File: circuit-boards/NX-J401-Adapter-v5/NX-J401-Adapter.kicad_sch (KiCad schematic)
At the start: 20 parts, among them J1 18V_OUT, J2 NX BUTTON, J3 Power, SW1 RECOVERY, SW2 RESET

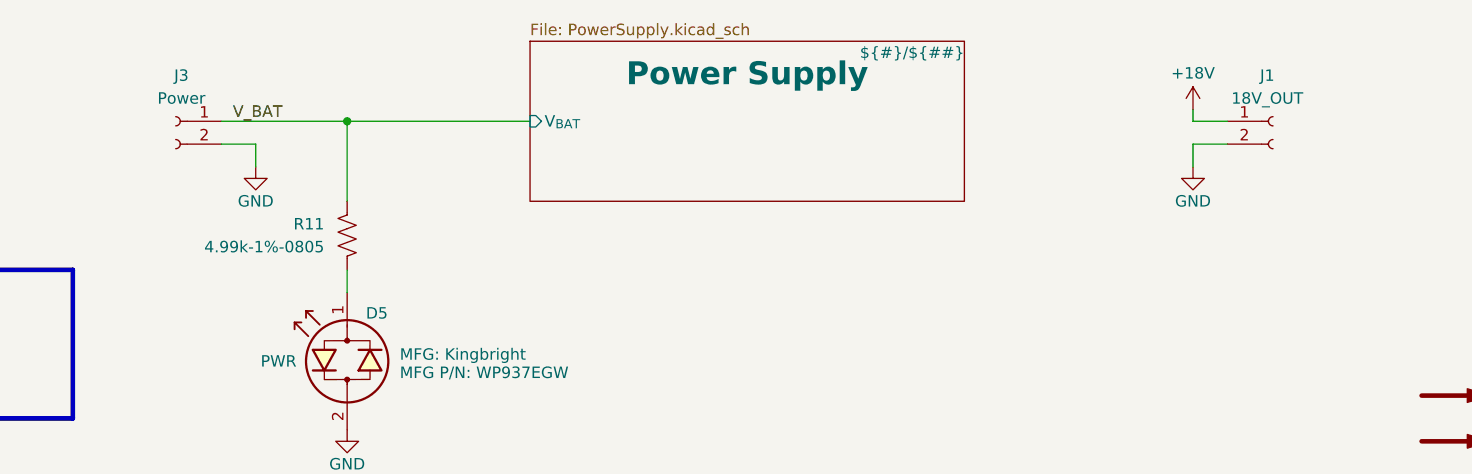
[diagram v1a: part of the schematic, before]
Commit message: Add over voltage protection to NX adapter circuit. Also reduce component height
Signed-off-by: Scott Berman <sgberman1@gmail.com>
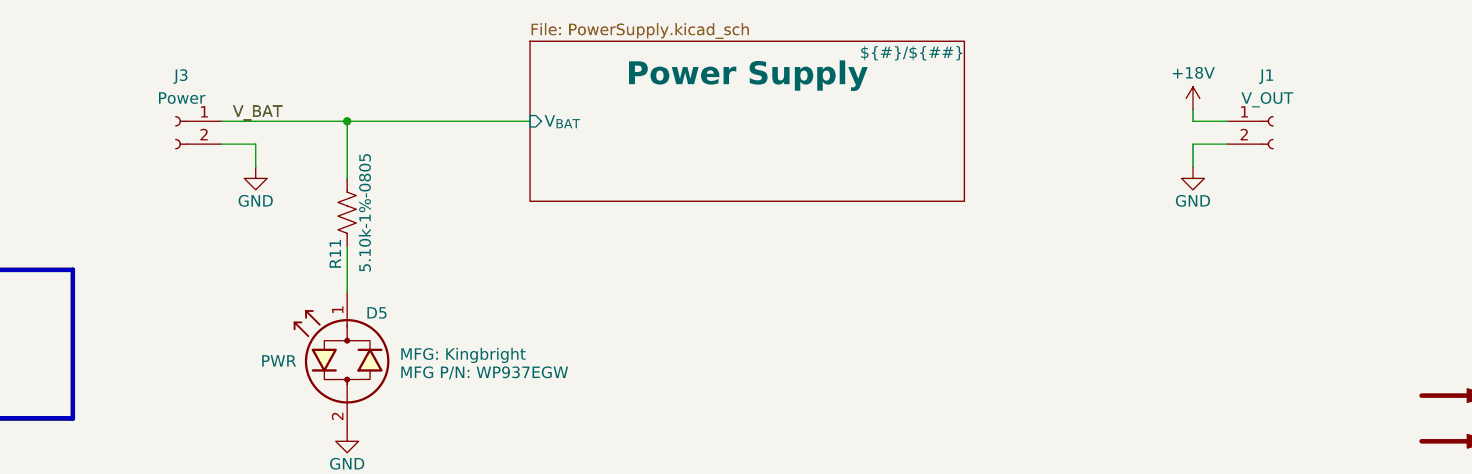
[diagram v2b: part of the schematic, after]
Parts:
- J1: value 18V_OUT -> V_OUT; footprint NX-J401-Adapter:CONN_69140872_WRE -> NX-J401-Adapter:Weidmuller-1824740000; DIST P/N 732-691408720002B-ND -> 281-2110-ND; MFG Würth Elektronik -> Weidmuller; MFG P/N 691408720002B -> 1824740000
- J3: footprint NX-J401-Adapter:Wurth-691406510002B -> NX-J401-Adapter:Weidmuller-1824740000; DIST P/N 732-691406510002B-ND -> 281-2110-ND; MFG Wurth -> Weidmuller; MFG P/N 691406510002B -> 1824740000
- R11: value 4.99k-1%-0805 -> 5.10k-1%-0805; DIST P/N 311-499CRCT-ND -> 311-5.10KCRCT-ND; MFG P/N RC0805FR-07499RL -> RC0805FR-075K1L
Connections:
- net V_BAT: now also R11.1; no longer R11.2
- net at D5.1 (KA): now also R11.2; no longer R11.1
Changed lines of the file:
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@@
 	(wire
 		(pts
-			(xy 161.29 73.66) (xy 161.29 82.55)
+			(xy 161.29 73.66) (xy 161.29 80.01)
 		)
 		(stroke
@@
 	(wire
 		(pts
-			(xy 161.29 90.17) (xy 161.29 92.71)
+			(xy 161.29 87.63) (xy 161.29 92.71)
 		)
 		(stroke
@@
 	)
 	(symbol
-		(lib_id "Device:R_US")
-		(at 161.29 86.36 0)
-		(mirror x)
-		(unit 1)
-		(exclude_from_sim no)
-		(in_bom yes)
-		(on_board yes)
-		(dnp no)
-		(property "Reference" "R11"
-			(at 158.75 85.09 0)
-			(effects
-				(font
-					(size 1.27 1.27)
-				)
-				(justify right)
-			)
-		)
-		(property "Value" "4.99k-1%-0805"
-			(at 158.75 87.63 0)
-			(effects
-				(font
-					(size 1.27 1.27)
-				)
-				(justify right)
-			)
-		)
-		(property "Footprint" "Resistor_SMD:R_0805_2012Metric"
-			(at 162.306 86.106 90)
-			(effects
-				(font
-					(size 1.27 1.27)
-				)
-				(hide yes)
-			)
-		)
-		(property "Datasheet" "Components/YageoPYu-RC_Group_51_RoHS_L_12.pdf"
-			(at 161.29 86.36 0)
-			(effects
-				(font
-					(size 1.27 1.27)
-				)
-				(hide yes)
-			)
-		)
-		(property "Description" ""
-			(at 161.29 86.36 0)
-			(effects
-				(font
-					(size 1.27 1.27)
-				)
-				(hide yes)
-			)
-		)
-		(property "MFG" "Yageo"
-			(at 161.29 86.36 0)
-			(effects
-				(font
-					(size 1.27 1.27)
-				)
-				(hide yes)
-			)
-		)
-		(property "MFG P/N" "RC0805FR-07499RL"
-			(at 161.29 86.36 0)
-			(effects
-				(font
-					(size 1.27 1.27)
-				)
-				(hide yes)
-			)
-		)
-		(property "DIST" "Digikey"
-			(at 161.29 86.36 0)
-			(effects
-				(font
-					(size 1.27 1.27)
-				)
-				(hide yes)
-			)
-		)
-		(property "DIST P/N" "311-499CRCT-ND"
-			(at 161.29 86.36 0)
-			(effects
-				(font
-					(size 1.27 1.27)
-				)
-				(hide yes)
-			)
-		)
-		(pin "1"
-		)
-		(pin "2"
-		)
-		(instances
-			(project "PI-Power-Board"
-				(path "/2707d6e5-f0fd-4132-ae41-e0b291f42ef6/feeb2d6c-4828-41f4-95de-5c15de403137"
-					(reference "R17")
-					(unit 1)
-				)
-			)
-			(project "NX-J401-Adapter"
-				(path "/cc31ce4b-09ab-4aea-a1d3-ed84696ba658"
-					(reference "R11")
-					(unit 1)
-				)
-			)
-		)
-	)
-	(symbol
 		(lib_id "Device:LED_Dual_Bidirectional")
 		(at 161.29 100.33 90)
@@
 	)
 	(symbol
+		(lib_id "Connector:Conn_01x02_Socket")
+		(at 264.16 73.66 0)
+		(unit 1)
+		(exclude_from_sim no)
+		(in_bom yes)
+		(on_board yes)
+		(dnp no)
+		(property "Reference" "J1"
+			(at 263.525 68.58 0)
+			(effects
+				(font
+					(size 1.27 1.27)
+				)
+			)
+		)
+		(property "Value" "V_OUT"
+			(at 263.525 71.12 0)
+			(effects
+				(font
+					(size 1.27 1.27)
+				)
+			)
+		)
+		(property "Footprint" "NX-J401-Adapter:Weidmuller-1824740000"
+			(at 264.16 73.66 0)
+			(effects
+				(font
+					(size 1.27 1.27)
+				)
+				(hide yes)
+			)
+		)
+		(property "Datasheet" "Components/Wurth-0691406510002B.pdf"
+			(at 264.16 73.66 0)
+			(effects
+				(font
+					(size 1.27 1.27)
+				)
+				(hide yes)
+			)
+		)
+		(property "Description" ""
+			(at 264.16 73.66 0)
+			(effects
+				(font
+					(size 1.27 1.27)
+				)
+				(hide yes)
+			)
+		)
+		(property "MFG" "Weidmuller"
+			(at 264.16 73.66 0)
+			(effects
+				(font
+					(size 1.27 1.27)
+				)
+				(hide yes)
+			)
+		)
+		(property "MFG P/N" "1824740000"
+			(at 264.16 73.66 0)
+			(effects
+				(font
+					(size 1.27 1.27)
+				)
+				(hide yes)
+			)
+		)
+		(property "DIST" "Digikey"
+			(at 264.16 73.66 0)
+			(effects
+				(font
+					(size 1.27 1.27)
+				)
+				(hide yes)
+			)
+		)
+		(property "DIST P/N" "281-2110-ND"
+			(at 264.16 73.66 0)
+			(effects
+				(font
+					(size 1.27 1.27)
+				)
+				(hide yes)
+			)
+		)
+		(pin "1"
+		)
+		(pin "2"
+		)
+		(instances
+			(project "NX-J401-Adapter"
+				(path "/cc31ce4b-09ab-4aea-a1d3-ed84696ba658"
+					(reference "J1")
+					(unit 1)
+				)
+			)
+		)
+	)
+	(symbol
 		(lib_id "Graphic:SYM_Arrow_Large")
 		(at 284.48 114.3 0)
@@
 	)
 	(symbol
+		(lib_id "Device:R_US")
+		(at 161.29 83.82 0)
+		(unit 1)
+		(exclude_from_sim no)
+		(in_bom yes)
+		(on_board yes)
+		(dnp no)
+		(property "Reference" "R11"
+			(at 160.02 88.392 90)
+			(effects
+				(font
+					(size 1.27 1.27)
+				)
+			)
+		)
+		(property "Value" "5.10k-1%-0805"
+			(at 163.322 83.82 90)
+			(effects
+				(font
+					(size 1.27 1.27)
+				)
+			)
+		)
+		(property "Footprint" "Resistor_SMD:R_0805_2012Metric"
+			(at 162.306 84.074 90)
+			(effects
+				(font
+					(size 1.27 1.27)
+				)
+				(hide yes)
+			)
+		)
+		(property "Datasheet" "Components/YageoPYu-RC_Group_51_RoHS_L_12.pdf"
+			(at 161.29 83.82 0)
+			(effects
+				(font
+					(size 1.27 1.27)
+				)
+				(hide yes)
+			)
+		)
+		(property "Description" ""
+			(at 161.29 83.82 0)
+			(effects
+				(font
+					(size 1.27 1.27)
+				)
+				(hide yes)
+			)
+		)
+		(property "MFG" "Yageo"
+			(at 161.29 83.82 0)
+			(effects
+				(font
+					(size 1.27 1.27)
+				)
+				(hide yes)
+			)
+		)
+		(property "MFG P/N" "RC0805FR-075K1L"
+			(at 161.29 83.82 0)
+			(effects
+				(font
+					(size 1.27 1.27)
+				)
+				(hide yes)
+			)
+		)
+		(property "DIST" "Digikey"
+			(at 161.29 83.82 0)
+			(effects
+				(font
+					(size 1.27 1.27)
+				)
+				(hide yes)
+			)
+		)
+		(property "DIST P/N" "311-5.10KCRCT-ND"
+			(at 161.29 83.82 0)
+			(effects
+				(font
+					(size 1.27 1.27)
+				)
+				(hide yes)
+			)
+		)
+		(pin "1"
+		)
+		(pin "2"
+		)
+		(instances
+			(project "NX-J401-Adapter"
+				(path "/cc31ce4b-09ab-4aea-a1d3-ed84696ba658"
+					(reference "R11")
+					(unit 1)
+				)
+			)
+		)
+	)
+	(symbol
 		(lib_id "power:GND")
 		(at 255.27 78.74 0)
@@
 			)
 		)
-		(property "Footprint" "NX-J401-Adapter:Wurth-691406510002B"
+		(property "Footprint" "NX-J401-Adapter:Weidmuller-1824740000"
 			(at 142.24 73.66 0)
 			(effects
@@
 			)
 		)
-		(property "MFG" "Wurth"
+		(property "MFG" "Weidmuller"
 			(at 142.24 73.66 0)
 			(effects
@@
 			)
 		)
-		(property "MFG P/N" "691406510002B"
+		(property "MFG P/N" "1824740000"
 			(at 142.24 73.66 0)
 			(effects
@@
 			)
 		)
-		(property "DIST P/N" "732-691406510002B-ND"
+		(property "DIST P/N" "281-2110-ND"
 			(at 142.24 73.66 0)
 			(effects
@@
 					(unit 1)
 				)
-			)
-		)
-	)
-	(symbol
-		(lib_id "Connector:Conn_01x02_Socket")
-		(at 264.16 73.66 0)
-		(unit 1)
-		(exclude_from_sim no)
-		(in_bom yes)
-		(on_board yes)
-		(dnp no)
-		(property "Reference" "J1"
-			(at 263.525 68.58 0)
-			(effects
-				(font
-					(size 1.27 1.27)
-				)
-			)
-		)
-		(property "Value" "18V_OUT"
-			(at 263.525 71.12 0)
-			(effects
-				(font
-					(size 1.27 1.27)
-				)
-			)
-		)
-		(property "Footprint" "NX-J401-Adapter:CONN_69140872_WRE"
-			(at 264.16 73.66 0)
-			(effects
-				(font
-					(size 1.27 1.27)
-				)
-				(hide yes)
-			)
-		)
-		(property "Datasheet" "Components/Wurth-691408720002B.pdf"
-			(at 264.16 73.66 0)
-			(effects
-				(font
-					(size 1.27 1.27)
-				)
-				(hide yes)
-			)
-		)
-		(property "Description" ""
-			(at 264.16 73.66 0)
-			(effects
-				(font
-					(size 1.27 1.27)
-				)
-				(hide yes)
-			)
-		)
-		(property "MFG" "Würth Elektronik"
-			(at 264.16 73.66 0)
-			(effects
-				(font
-					(size 1.27 1.27)
-				)
-				(hide yes)
-			)
-		)
-		(property "MFG P/N" "691408720002B"
-			(at 264.16 73.66 0)
-			(effects
-				(font
-					(size 1.27 1.27)
-				)
-				(hide yes)
-			)
-		)
-		(property "DIST" "Digikey"
-			(at 264.16 73.66 0)
-			(effects
-				(font
-					(size 1.27 1.27)
-				)
-				(hide yes)
-			)
-		)
-		(property "DIST P/N" "732-691408720002B-ND"
-			(at 264.16 73.66 0)
-			(effects
-				(font
-					(size 1.27 1.27)
-				)
-				(hide yes)
-			)
-		)
-		(pin "1"
-		)
-		(pin "2"
-		)
-		(instances
-			(project "NX-J401-Adapter"
-				(path "/cc31ce4b-09ab-4aea-a1d3-ed84696ba658"
-					(reference "J1")
-					(unit 1)
-				)

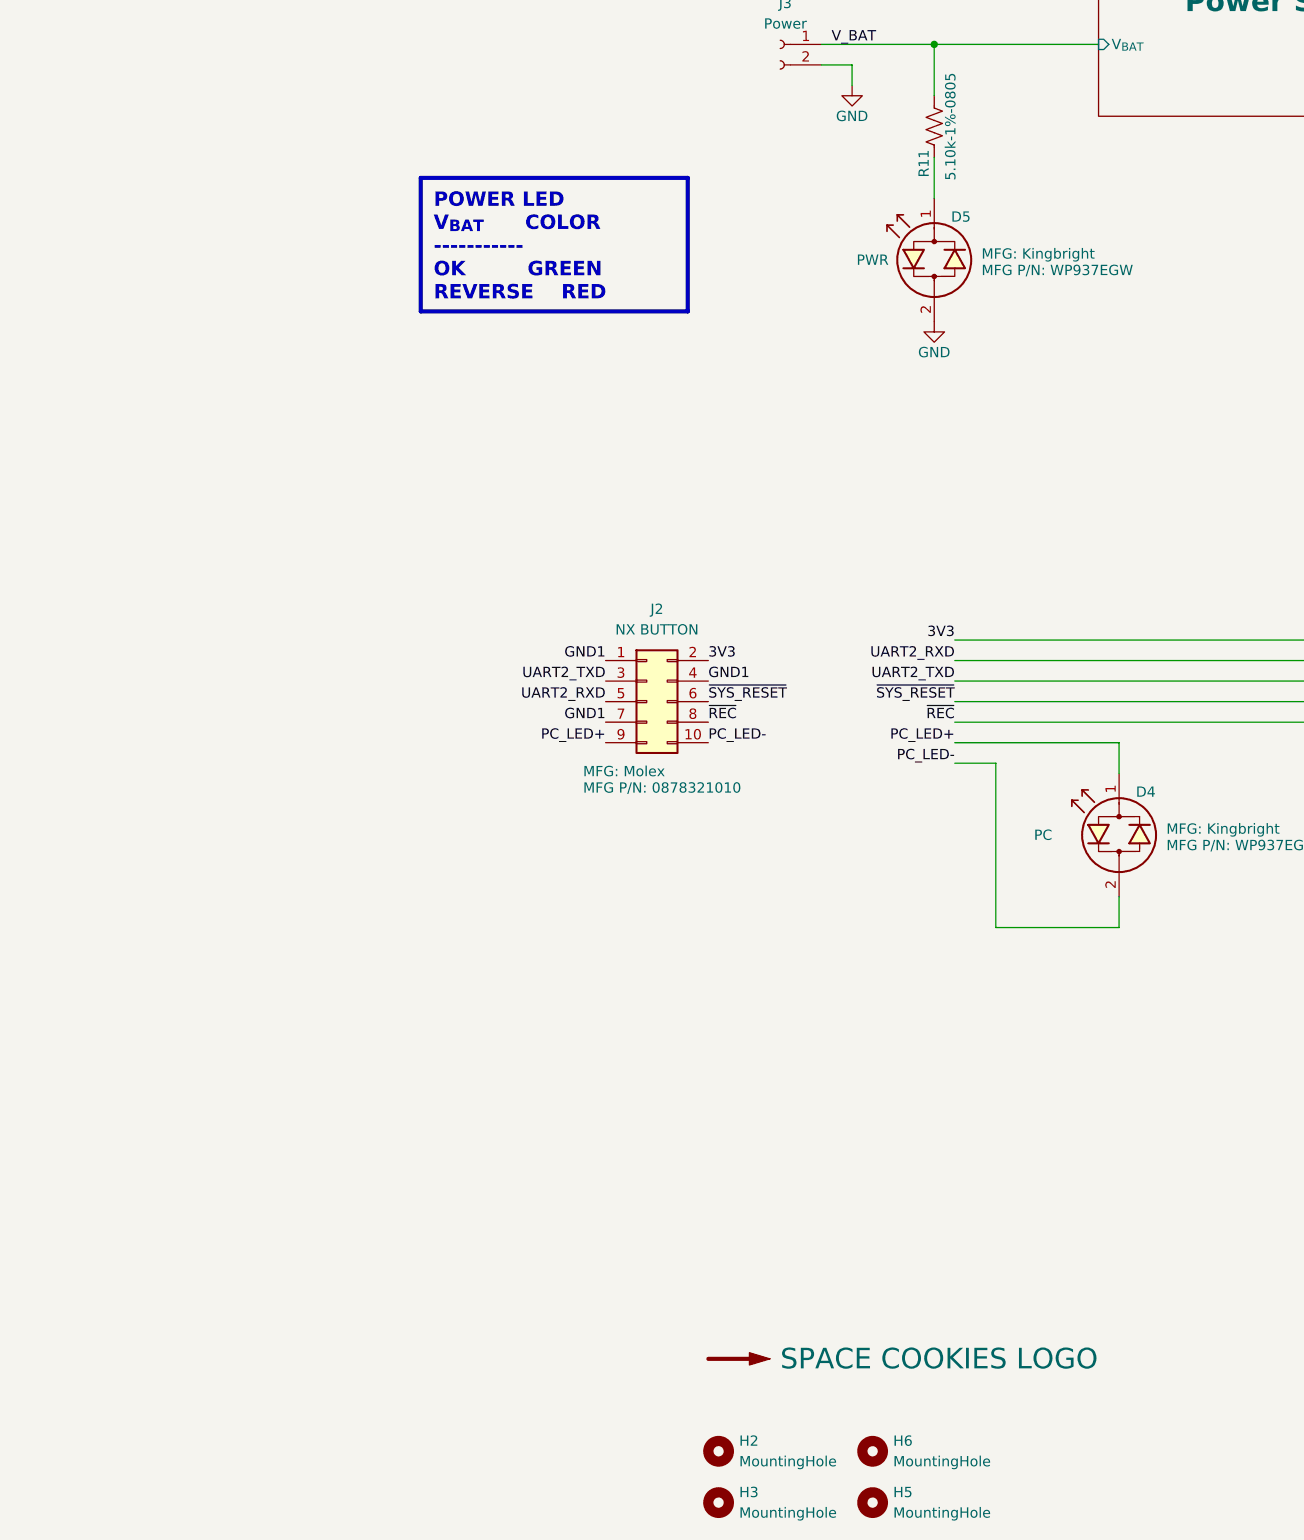
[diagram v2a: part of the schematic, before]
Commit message: Change NX-J401-Adapter to reduce the PCB standoff spacing.
Signed-off-by: Scott Berman <sgberman1@gmail.com>
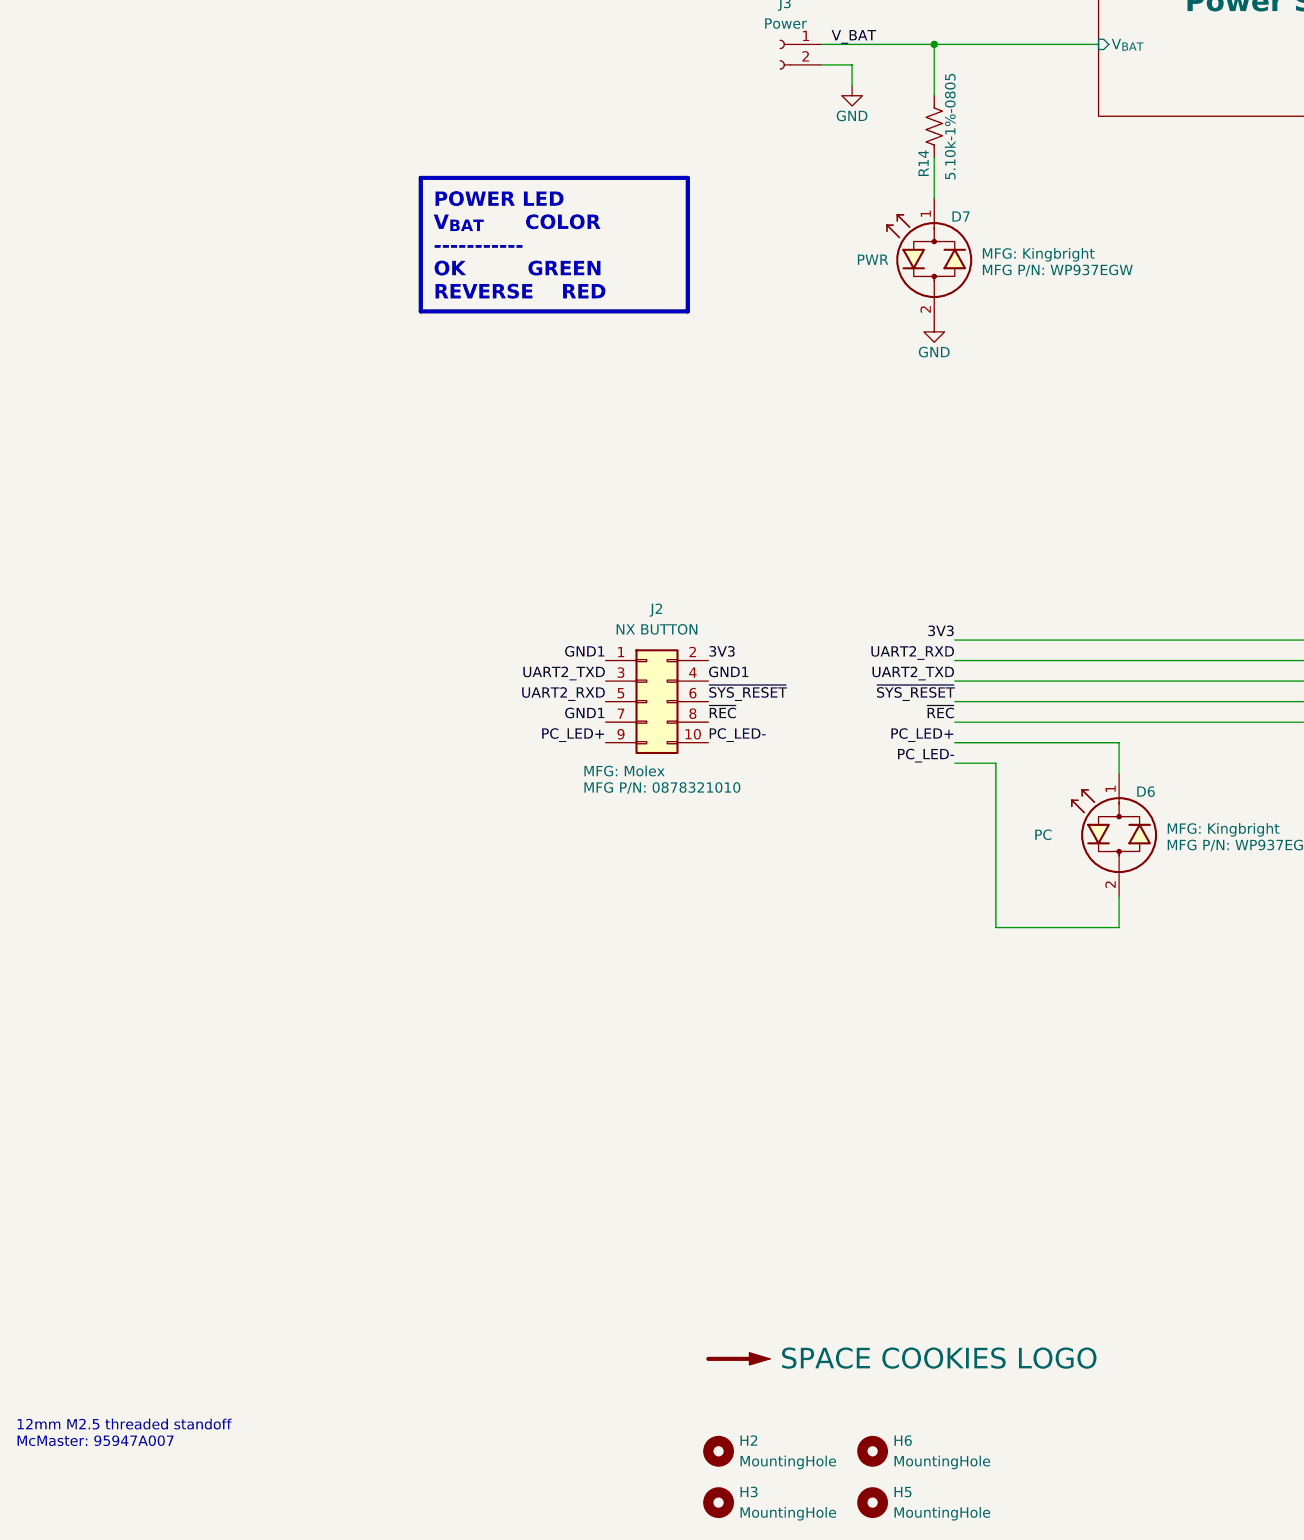
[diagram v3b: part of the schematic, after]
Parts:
- renumbered D4 to D6, D5 to D7, R11 to R14
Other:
- note added: "12mm M2.5 threaded standoff McMaster: 95947A007"
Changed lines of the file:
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@@
 	(title_block
 		(title "NX J401 Adapter")
-		(date "2025-09-13")
+		(date "2025-10-19")
 		(rev "5")
+	)
+	(text "12mm M2.5 threaded standoff \nMcMaster: 95947A007"
+		(exclude_from_sim no)
+		(at 47.752 245.618 0)
+		(effects
+			(font
+				(size 1.27 1.27)
+			)
+			(justify left)
+			(href "https://www.mcmaster.com/95947A007/")
+		)
 	)
 	(text "Spacer - OD: 4mm\nScrew  - M2 - 1.9mm OD\n\n"
@@
 		(on_board yes)
 		(dnp no)
-		(property "Reference" "D5"
+		(property "Reference" "D7"
 			(at 164.592 94.996 90)
 			(effects
@@
 			(project ""
 				(path "/cc31ce4b-09ab-4aea-a1d3-ed84696ba658"
-					(reference "D5")
+					(reference "D7")
 					(unit 1)
 				)
@@
 			)
 		)
-		(property "Datasheet" "Components/Wurth-0691406510002B.pdf"
+		(property "Datasheet" "Components/Weidmuller-1824740000.pdf"
 			(at 264.16 73.66 0)
 			(effects
@@
 		(on_board yes)
 		(dnp no)
-		(property "Reference" "R11"
+		(property "Reference" "R14"
 			(at 160.02 88.392 90)
 			(effects
@@
 			(project "NX-J401-Adapter"
 				(path "/cc31ce4b-09ab-4aea-a1d3-ed84696ba658"
-					(reference "R11")
+					(reference "R14")
 					(unit 1)
 				)
@@
 		(on_board yes)
 		(dnp no)
-		(property "Reference" "D4"
+		(property "Reference" "D6"
 			(at 187.452 166.116 90)
 			(effects
@@
 			(project "NX-J401-Adapter"
 				(path "/cc31ce4b-09ab-4aea-a1d3-ed84696ba658"
-					(reference "D4")
+					(reference "D6")
 					(unit 1)
 				)
@@
 			)
 		)
-		(property "Datasheet" "Components/Wurth-0691406510002B.pdf"
+		(property "Datasheet" "Components/Weidmuller-1824740000.pdf"
 			(at 142.24 73.66 0)
 			(effects
